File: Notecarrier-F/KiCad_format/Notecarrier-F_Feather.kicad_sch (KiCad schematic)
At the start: 0 parts

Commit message: Port Notecarrier-F schematic and BOM.
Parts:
- added J7, J8: SM04B-SRSS-TB(LF)(SN), symbol Connector_Generic:Conn_01x04
- added MOD1L1: Conn_01x16, symbol Connector_Generic:Conn_01x16
- added MOD1R1: Conn_01x12, symbol Connector_Generic:Conn_01x12
- added MOD2: Feather Module, symbol blues-kicad-lib:FeatherModule
- added R3 (x2): 10k, symbol Device:R
- added SW3: PTS810-SJS-250-SMTR-LFS, blues-kicad-lib:PTS810-SJS-250-SMTR-LFS, symbol blues-kicad-lib:PTS810-SJS-250-SMTR-LFS
- added SW4, SW5: CJS-1200TA, blues-kicad-lib:CJS-1200TA, symbol blues-kicad-lib:CJS-1200TA
- added TP1: ~, symbol Connector:TestPoint
- added U4: TXS0102DCU, Package_SO:VSSOP-8_2.3x2mm_P0.5mm, symbol blues-kicad-lib:TXS0102DCU
- added U6: DGQ2788AEN-T1-GE4, symbol blues-kicad-lib:DGQ2788AEN-T1-GE4
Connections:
- new net DFU_SW: SW4.2 (B), U6.14 (IN1-2), U6.6 (IN3-4)
- new net EN_F_BAT: SW4.3 (A), SW5.2 (B), U4.6 (OE), U6.10 (V+)
- new net F_3V3: J7.3 (Pin_3), J8.3 (Pin_3), MOD1L1.2 (Pin_2), R3.1, R3.1, U4.7 (VCCB)
- new net F_A0: MOD1L1.5 (Pin_5)
- new net F_A1: MOD1L1.6 (Pin_6)
- new net F_A2: MOD1L1.7 (Pin_7)
- new net F_A3: MOD1L1.8 (Pin_8)
- new net F_A4: MOD1L1.9 (Pin_9)
- new net F_A5: MOD1L1.10 (Pin_10)
- new net F_AREF: MOD1L1.3 (Pin_3)
- new net F_B0: MOD1L1.16 (Pin_16), U6.16 (COM2)
- new net F_B0_SW: SW3.3, SW3.4, U6.1 (NC2)
- new net F_BAT: MOD1R1.1 (Pin_1)
- new net F_D10: MOD1R1.7 (Pin_7)
- new net F_D11: MOD1R1.6 (Pin_6)
- new net F_D12: MOD1R1.5 (Pin_5)
- new net F_D13: MOD1R1.4 (Pin_4)
- new net F_D5: MOD1R1.10 (Pin_10)
- new net F_D6: MOD1R1.9 (Pin_9)
- new net F_D9: MOD1R1.8 (Pin_8)
- new net F_EN: MOD1R1.2 (Pin_2)
- new net F_MISO: MOD1L1.13 (Pin_13)
- new net F_MOSI: MOD1L1.12 (Pin_12)
- new net F_NRST: MOD1L1.1 (Pin_1), U6.12 (COM1)
- new net F_NRST_SW: U6.13 (NC1)
- new net F_RX: MOD1L1.14 (Pin_14), U6.8 (COM4)
- new net F_RX_SW: U6.9 (NC4)
- new net F_SCK: MOD1L1.11 (Pin_11)
- new net F_SCL: J7.1 (Pin_1), J8.1 (Pin_1), MOD1R1.11 (Pin_11), R3.2, U4.1 (B2)
- new net F_SDA: J7.2 (Pin_2), J8.2 (Pin_2), MOD1R1.12 (Pin_12), R3.2, U4.8 (B1)
- new net F_TX: MOD1L1.15 (Pin_15), U6.4 (COM3)
- new net F_TX_SW: U6.5 (NC3)
- new net F_VUSB: MOD1R1.3 (Pin_3)
- new net GND: J7.4 (Pin_4), J8.4 (Pin_4), MOD1L1.4 (Pin_4), SW3.1, SW3.2, SW4.1 (C), U4.2 (GND), U6.2 (GND)
- new net N_ATTN: SW5.1 (C)
- new net N_AUX3: TP1.1, U6.15 (NO2)
- new net N_AUX4: U6.11 (NO1)
- new net N_AUX_RX: U6.3 (NO3)
- new net N_AUX_TX: U6.7 (NO4)
- new net N_SCL: U4.4 (A2)
- new net N_SDA: U4.5 (A1)
- new net N_VIO: SW5.3 (A), U4.3 (VCCA)
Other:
- note added: "ATTN MODE ENABLE"
- note added: "DFU ENABLE"
- note added: "FEATHER"
- note added: "FLICK SWITCH TOWARDS THE TEXT "ON" TO ENABLE OUTBOARD DFU"
- note added: "Feather Module Connector"
- note added: "Feather PWR flicked towards the text ON means "ATTN MODE" IS OFF"
- note added: "I2C Level Shifter"
- note added: "Label Promotion"
- note added: "NOTECARD OR IO HEADER"
- note added: "ON"
- note added: "Qwiic Connectors"
- note added: "SWITCHED"
- note added: "Several of the net labels on this sheet need to be common with other sheets. In the original Altium source files, this was achieved for some labels by adding Off-Sheet Connectors to the nets. But the remainder (inadvertently perhaps) rely on promoting all net labels to global using the "Net Identifier Scope" setting. This renders the original Off Sheet Connectors redundant. To avoid losing that d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"
- note added: "TRUTH TABLE: IN1-2, IN3-4 LOGIC 0 = NC is TRUE/HIGH DFU=N LOGIC 1 = NO is TRUE/HIGH DFU=Y"
- note added: "USER"
- title: (none) -> Notecarrier-F

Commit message: Ported footprint assignments, board outline, copper layers and dimensional drawings for Notecarrier-F.
Footprints currently held in a “blues-kicad-lib-pending” library, prior to merging with “blues-kicad-lib” and deleting unused items.
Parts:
- J7, J8: footprint (none) -> blues-kicad-lib-pending:JST SM04B-SRSS-TB
- MOD1L1: footprint (none) -> blues-kicad-lib-pending:16PIN_254MM
- MOD1R1: footprint (none) -> blues-kicad-lib-pending:12PIN_254MM
- R3: footprint (none) -> blues-kicad-lib-pending:RES 0402_1005
- SW3: footprint blues-kicad-lib:PTS810-SJS-250-SMTR-LFS -> blues-kicad-lib-pending:C&K PTS810
- SW4, SW5: footprint blues-kicad-lib:CJS-1200TA -> blues-kicad-lib-pending:SW_CJS-1200TA
- TP1: footprint (none) -> blues-kicad-lib-pending:TESTPAD_127
- U4: footprint Package_SO:VSSOP-8_2.3x2mm_P0.5mm -> blues-kicad-lib-pending:SOP50P310X90-8N
- U6: footprint (none) -> blues-kicad-lib-pending:QFN40P260X180X60-16N
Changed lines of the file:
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@@
       (effects (font (size 1.27 1.27)))
     )
-    (property "Footprint" "" (at 134.62 120.65 0)
+    (property "Footprint" "blues-kicad-lib-pending:JST SM04B-SRSS-TB" (at 134.62 120.65 0)
       (effects (font (size 1.27 1.27)) hide)
     )
@@
       (effects (font (size 1.27 1.27)) (justify right))
     )
-    (property "Footprint" "blues-kicad-lib:CJS-1200TA" (at 106.68 54.61 0)
+    (property "Footprint" "blues-kicad-lib-pending:SW_CJS-1200TA" (at 106.68 54.61 0)
       (effects (font (size 1.27 1.27)) hide)
     )
@@
       (effects (font (size 1.27 1.27)))
     )
-    (property "Footprint" "blues-kicad-lib:PTS810-SJS-250-SMTR-LFS" (at 53.34 95.25 0)
+    (property "Footprint" "blues-kicad-lib-pending:C&K PTS810" (at 53.34 95.25 0)
       (effects (font (size 1.27 1.27)) hide)
     )
@@
       (effects (font (size 1.27 1.27)) (justify right))
     )
-    (property "Footprint" "blues-kicad-lib:CJS-1200TA" (at 227.33 266.7 0)
+    (property "Footprint" "blues-kicad-lib-pending:SW_CJS-1200TA" (at 227.33 266.7 0)
       (effects (font (size 1.27 1.27)) hide)
     )
@@
       (effects (font (size 1.27 1.27)) (justify left))
     )
-    (property "Footprint" "" (at 165.1 36.195 90)
+    (property "Footprint" "blues-kicad-lib-pending:QFN40P260X180X60-16N" (at 165.1 36.195 90)
       (effects (font (size 1.27 1.27)) hide)
     )
@@
       (effects (font (size 1.27 1.27)) hide)
     )
-    (property "Footprint" "" (at 130.81 187.96 0)
+    (property "Footprint" "blues-kicad-lib-pending:12PIN_254MM" (at 130.81 187.96 0)
       (effects (font (size 1.27 1.27)) hide)
     )
@@
       (effects (font (size 1.27 1.27)) (justify left) hide)
     )
-    (property "Footprint" "" (at 100.33 182.88 0)
+    (property "Footprint" "blues-kicad-lib-pending:16PIN_254MM" (at 100.33 182.88 0)
       (effects (font (size 1.27 1.27)) hide)
     )
@@
       (effects (font (size 1.27 1.27)) (justify left))
     )
-    (property "Footprint" "" (at 239.522 105.41 90)
+    (property "Footprint" "blues-kicad-lib-pending:RES 0402_1005" (at 239.522 105.41 90)
       (effects (font (size 1.27 1.27)) hide)
     )
@@
       (effects (font (size 1.27 1.27)) (justify left))
     )
-    (property "Footprint" "" (at 207.01 40.64 0)
+    (property "Footprint" "blues-kicad-lib-pending:TESTPAD_127" (at 207.01 40.64 0)
       (effects (font (size 1.27 1.27)) hide)
     )
@@
       (effects (font (size 1.27 1.27)) (justify left))
     )
-    (property "Footprint" "Package_SO:VSSOP-8_2.3x2mm_P0.5mm" (at 99.06 276.86 0)
+    (property "Footprint" "blues-kicad-lib-pending:SOP50P310X90-8N" (at 99.06 276.86 0)
       (effects (font (size 1.27 1.27)) hide)
     )
@@
       (effects (font (size 1.27 1.27)) (justify left))
     )
-    (property "Footprint" "" (at 234.442 105.41 90)
+    (property "Footprint" "blues-kicad-lib-pending:RES 0402_1005" (at 234.442 105.41 90)
       (effects (font (size 1.27 1.27)) hide)
     )
@@
       (effects (font (size 1.27 1.27)))
     )
-    (property "Footprint" "" (at 175.26 120.65 0)
-      (effects (font (size 1.27 1.27)) hide)
-    )
+    (property "Footprint" "blues-kicad-lib-pending:JST SM04B-SRSS-TB" (at 175.26 120.65 0)
+      (effects (font (size 1.27 1.27)) hide)
+    )

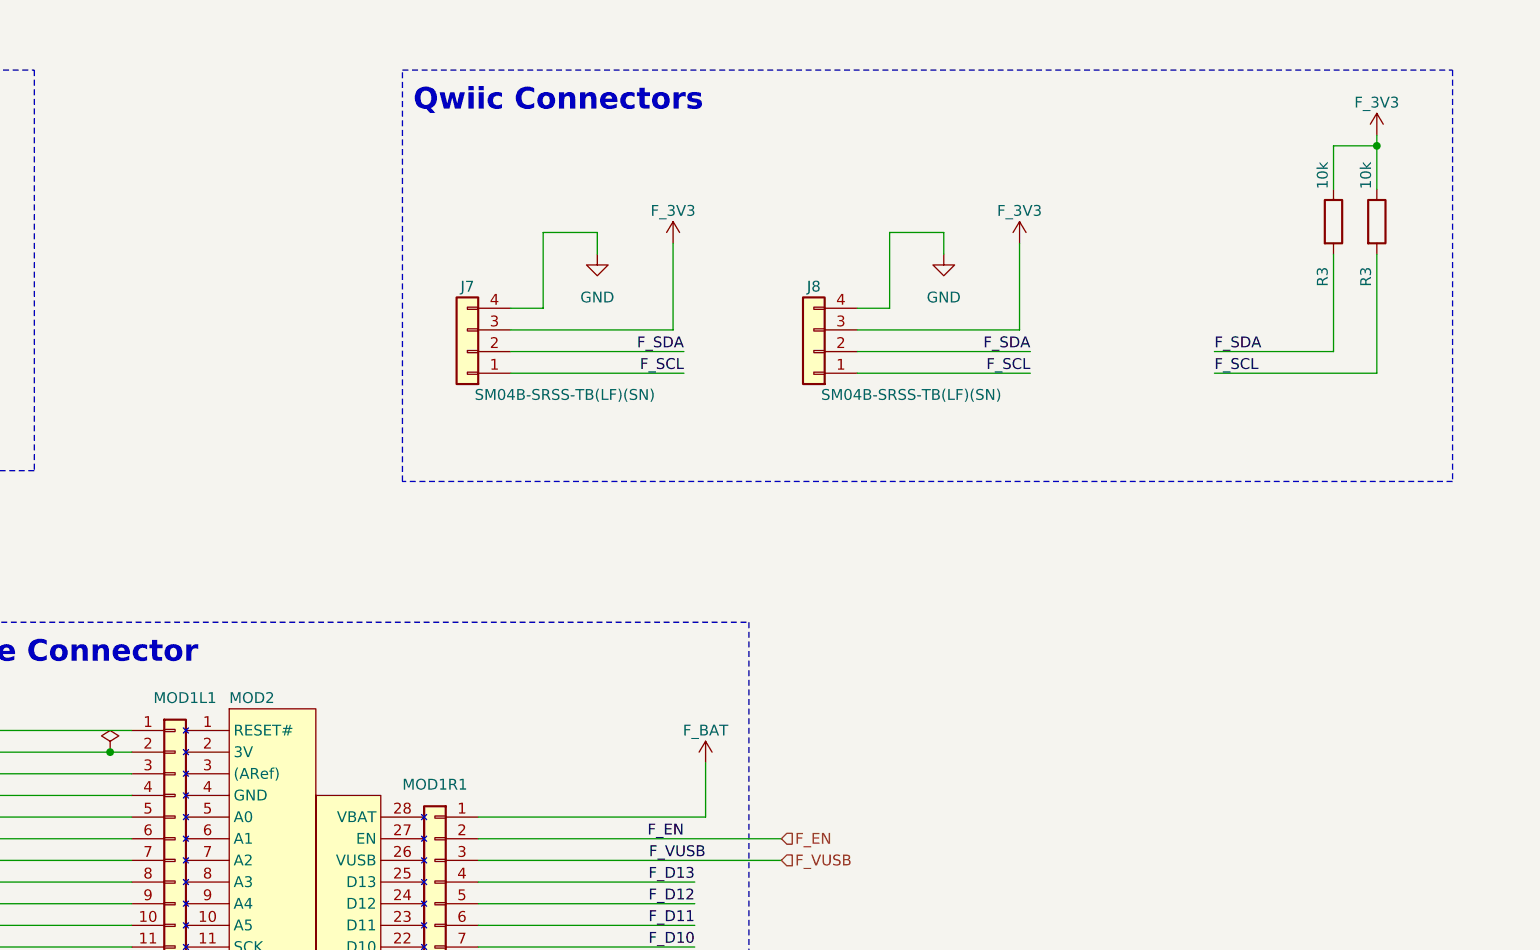
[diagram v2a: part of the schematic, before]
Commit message: Finish first pass PCB port.
Still need to go back and finalise top-level schematic sheet.
Next step is validation where there’s bound to be lots of copper rules to tweak.
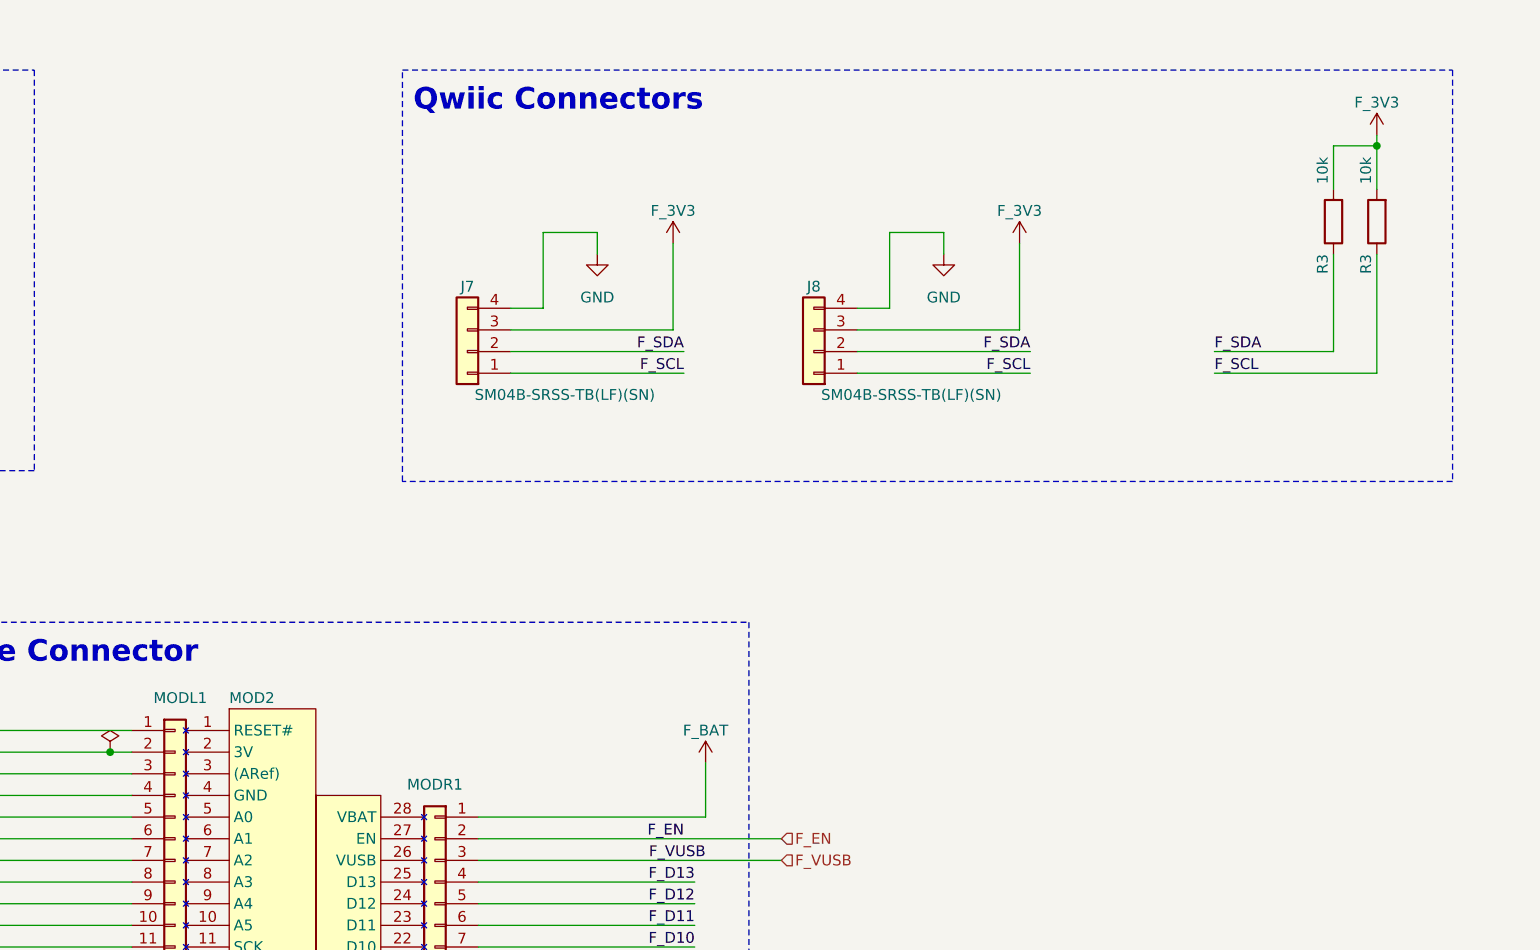
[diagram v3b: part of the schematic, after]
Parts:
- MOD2: footprint (none) -> blues-kicad-lib-pending:BLUES_WIRELESS_SWAN_2-54_HEADERS
- TP1: value ~ -> TESTPAD
- renumbered MOD1L1 to MODL1, MOD1R1 to MODR1
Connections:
- net F_3V3: now also R3.2, R3.2; no longer R3.1, R3.1
- net F_SCL: now also R3.1; no longer R3.2
- net F_SDA: now also R3.1; no longer R3.2
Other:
- moved on the sheet: R3
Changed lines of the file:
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@@
   (symbol (lib_id "Connector_Generic:Conn_01x12") (at 130.81 187.96 0) (mirror y) (unit 1)
     (in_bom yes) (on_board yes) (dnp no)
-    (property "Reference" "MOD1R1" (at 130.81 171.45 0)
+    (property "Reference" "MODR1" (at 130.81 171.45 0)
       (effects (font (size 1.27 1.27)))
     )
@@
     )
     (property "Part Number" "00536" (at 130.81 187.96 0)
+      (effects (font (size 1.27 1.27)) hide)
+    )
+    (property "Critical" "" (at 130.81 187.96 0)
+      (effects (font (size 1.27 1.27)) hide)
+    )
+    (property "Supplier" "" (at 130.81 187.96 0)
       (effects (font (size 1.27 1.27)) hide)
     )
@@
       (project "Notecarrier-F"
         (path "/3e57c059-f782-40ac-b9a3-c1636ed27a63/fb5887cf-5e51-4ae9-9749-dbe8e6b41d9d"
-          (reference "MOD1R1") (unit 1)
+          (reference "MODR1") (unit 1)
         )
       )
@@
       (effects (font (size 1.27 1.27)) (justify left))
     )
-    (property "Footprint" "" (at 116.84 194.31 0)
+    (property "Footprint" "blues-kicad-lib-pending:BLUES_WIRELESS_SWAN_2-54_HEADERS" (at 116.84 194.31 0)
       (effects (font (size 1.27 1.27)) hide)
     )
     (property "Datasheet" "" (at 116.84 196.85 0)
+      (effects (font (size 1.27 1.27)) hide)
+    )
+    (property "Critical" "" (at 116.84 185.42 0)
+      (effects (font (size 1.27 1.27)) hide)
+    )
+    (property "Description" "" (at 116.84 185.42 0)
+      (effects (font (size 1.27 1.27)) hide)
+    )
+    (property "Manufacturer" "" (at 116.84 185.42 0)
+      (effects (font (size 1.27 1.27)) hide)
+    )
+    (property "Order Code" "" (at 116.84 185.42 0)
+      (effects (font (size 1.27 1.27)) hide)
+    )
+    (property "Part Number" "" (at 116.84 185.42 0)
+      (effects (font (size 1.27 1.27)) hide)
+    )
+    (property "Supplier" "" (at 116.84 185.42 0)
       (effects (font (size 1.27 1.27)) hide)
     )
@@
   (symbol (lib_id "Connector_Generic:Conn_01x16") (at 100.33 182.88 0) (unit 1)
     (in_bom yes) (on_board yes) (dnp no)
-    (property "Reference" "MOD1L1" (at 97.79 161.29 0)
+    (property "Reference" "MODL1" (at 97.79 161.29 0)
       (effects (font (size 1.27 1.27)) (justify left))
     )
@@
     )
     (property "Part Number" "00542" (at 100.33 182.88 0)
+      (effects (font (size 1.27 1.27)) hide)
+    )
+    (property "Critical" "" (at 100.33 182.88 0)
+      (effects (font (size 1.27 1.27)) hide)
+    )
+    (property "Supplier" "" (at 100.33 182.88 0)
       (effects (font (size 1.27 1.27)) hide)
     )
@@
       (project "Notecarrier-F"
         (path "/3e57c059-f782-40ac-b9a3-c1636ed27a63/fb5887cf-5e51-4ae9-9749-dbe8e6b41d9d"
-          (reference "MOD1L1") (unit 1)
-        )
-      )
-    )
-  )
-  (symbol (lib_id "Device:R") (at 241.3 105.41 0) (unit 1)
+          (reference "MODL1") (unit 1)
+        )
+      )
+    )
+  )
+  (symbol (lib_id "Device:R") (at 241.3 105.41 180) (unit 1)
     (in_bom yes) (on_board yes) (dnp no)
-    (property "Reference" "R3" (at 240.03 113.03 90)
-      (effects (font (size 1.27 1.27)) (justify left))
-    )
-    (property "Value" "10k" (at 240.03 101.6 90)
-      (effects (font (size 1.27 1.27)) (justify left))
-    )
-    (property "Footprint" "blues-kicad-lib-pending:RES 0402_1005" (at 239.522 105.41 90)
+    (property "Reference" "R3" (at 240.03 109.22 90)
+      (effects (font (size 1.27 1.27)) (justify left))
+    )
+    (property "Value" "10k" (at 240.03 97.79 90)
+      (effects (font (size 1.27 1.27)) (justify left))
+    )
+    (property "Footprint" "blues-kicad-lib-pending:RES 0402_1005" (at 243.078 105.41 90)
       (effects (font (size 1.27 1.27)) hide)
     )
@@
       (effects (font (size 1.27 1.27)))
     )
-    (property "Value" "~" (at 204.47 39.243 0)
-      (effects (font (size 1.27 1.27)) (justify left))
+    (property "Value" "TESTPAD" (at 204.47 39.243 0)
+      (effects (font (size 1.27 1.27)) (justify left) hide)
     )
     (property "Footprint" "blues-kicad-lib-pending:TESTPAD_127" (at 207.01 40.64 0)
@@
     )
   )
-  (symbol (lib_id "Device:R") (at 236.22 105.41 0) (unit 1)
+  (symbol (lib_id "Device:R") (at 236.22 105.41 180) (unit 1)
     (in_bom yes) (on_board yes) (dnp no)
-    (property "Reference" "R3" (at 234.95 113.03 90)
-      (effects (font (size 1.27 1.27)) (justify left))
-    )
-    (property "Value" "10k" (at 234.95 101.6 90)
-      (effects (font (size 1.27 1.27)) (justify left))
-    )
-    (property "Footprint" "blues-kicad-lib-pending:RES 0402_1005" (at 234.442 105.41 90)
-      (effects (font (size 1.27 1.27)) hide)
-    )
+    (property "Reference" "R3" (at 234.95 109.22 90)
+      (effects (font (size 1.27 1.27)) (justify left))
+    )
+    (property "Value" "10k" (at 234.95 97.79 90)
+      (effects (font (size 1.27 1.27)) (justify left))
+    )
+    (property "Footprint" "blues-kicad-lib-pending:RES 0402_1005" (at 237.998 105.41 90)
+      (effects (font (size 1.27 1.27)) hide)
+    )
